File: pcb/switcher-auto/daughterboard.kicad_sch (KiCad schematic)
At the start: 6 parts, among them J0 MD-90SM, J1 MD-90SM, J2 MD-90SM, J3 MD-90SM, J4 MD-90SM, J5 Conn_02x22_Top_Bottom

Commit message: WIP routing as 4 layers with new connector organization
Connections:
- net 1_GND is gone; now on net 0_GND: J1.S1 (SHIELD), J1.S2 (SHIELD), J1.S3 (SHIELD), J5.16 (Pin_16)
- net 0_BVID: now also J5.6 (Pin_6); no longer J5.1 (Pin_1)
- net 0_CVID: now also J5.36 (Pin_36); no longer J5.4 (Pin_4)
- net 0_GND: now also J2.S1 (SHIELD), J2.S2 (SHIELD), J2.S3 (SHIELD), J3.S1 (SHIELD), J3.S2 (SHIELD), J3.S3 (SHIELD), J4.S1 (SHIELD), J4.S2 (SHIELD), J4.S3 (SHIELD), J5.17 (Pin_17), J5.18 (Pin_18), J5.19 (Pin_19), J5.20 (Pin_20); no longer J5.8 (Pin_8)
- net 0_GVID: now also J5.11 (Pin_11); no longer J5.2 (Pin_2)
- net 0_LAUD: now also J5.31 (Pin_31); no longer J5.5 (Pin_5)
- net 0_RAUD: now also J5.26 (Pin_26); no longer J5.6 (Pin_6)
- net 0_RVID: now also J5.1 (Pin_1); no longer J5.3 (Pin_3)
- net 1_BVID: now also J5.7 (Pin_7); no longer J5.9 (Pin_9)
- net 1_CVID: now also J5.37 (Pin_37); no longer J5.12 (Pin_12)
- net 1_GVID: now also J5.12 (Pin_12); no longer J5.10 (Pin_10)
- net 1_LAUD: now also J5.32 (Pin_32); no longer J5.13 (Pin_13)
- net 1_RAUD: now also J5.27 (Pin_27); no longer J5.14 (Pin_14)
- net 1_RVID: now also J5.2 (Pin_2); no longer J5.11 (Pin_11)
- net 2_BVID: now also J5.8 (Pin_8); no longer J5.33 (Pin_33)
- net 2_CVID: now also J5.38 (Pin_38); no longer J5.36 (Pin_36)
- net 2_GVID: now also J5.13 (Pin_13); no longer J5.34 (Pin_34)
- net 2_LAUD: now also J5.33 (Pin_33); no longer J5.37 (Pin_37)
- net 2_RAUD: now also J5.28 (Pin_28); no longer J5.38 (Pin_38)
- net 2_RVID: now also J5.3 (Pin_3); no longer J5.35 (Pin_35)
- net 3_BVID: now also J5.9 (Pin_9); no longer J5.25 (Pin_25)
- net 3_CVID: now also J5.39 (Pin_39); no longer J5.28 (Pin_28)
- net 3_GVID: now also J5.14 (Pin_14); no longer J5.26 (Pin_26)
- net 3_LAUD: now also J5.34 (Pin_34); no longer J5.29 (Pin_29)
- net 3_RAUD: now also J5.29 (Pin_29); no longer J5.30 (Pin_30)
- net 3_RVID: now also J5.4 (Pin_4); no longer J5.27 (Pin_27)
- net 4_BVID: now also J5.10 (Pin_10); no longer J5.17 (Pin_17)
- net 4_CVID: now also J5.40 (Pin_40); no longer J5.20 (Pin_20)
- net 4_GVID: now also J5.15 (Pin_15); no longer J5.18 (Pin_18)
- net 4_LAUD: now also J5.35 (Pin_35); no longer J5.21 (Pin_21)
- net 4_RAUD: now also J5.30 (Pin_30); no longer J5.22 (Pin_22)
- net 4_RVID: now also J5.5 (Pin_5); no longer J5.19 (Pin_19)
- net 0_5V renamed 0_VCC
- net 0_VCC: now also J5.21 (Pin_21); no longer J5.7 (Pin_7)
- net 1_5V renamed 1_VCC
- net 1_VCC: now also J5.22 (Pin_22); no longer J5.15 (Pin_15)
- net 2_5V renamed 2_VCC
- net 2_VCC: now also J5.23 (Pin_23); no longer J5.39 (Pin_39)
- removed net 2_GND: J2.S1 (SHIELD), J2.S2 (SHIELD), J2.S3 (SHIELD), J5.40 (Pin_40)
- net 3_5V renamed 3_VCC
- net 3_VCC: now also J5.24 (Pin_24); no longer J5.31 (Pin_31)
- removed net 3_GND: J3.S1 (SHIELD), J3.S2 (SHIELD), J3.S3 (SHIELD), J5.32 (Pin_32)
- net 4_5V renamed 4_VCC
- net 4_VCC: now also J5.25 (Pin_25); no longer J5.23 (Pin_23)
- removed net 4_GND: J4.S1 (SHIELD), J4.S2 (SHIELD), J4.S3 (SHIELD), J5.24 (Pin_24)

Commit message: Routing pt 2
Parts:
- added R1, R2, R3, R4, R5: R_Small, Resistor_SMD:R_0805_2012Metric_Pad1.20x1.40mm_HandSolder, symbol Device:R_Small
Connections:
- net 0_VCC: now also R5.1
- net 1_VCC: now also R4.1
- net 2_VCC: now also R3.1
- net 3_VCC: now also R2.1
- net 4_VCC: now also R1.1
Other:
- moved on the sheet: J4

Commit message: finish routing?
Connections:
- net 0_VCC: now also R5.2; no longer J5.21 (Pin_21), R5.1
- net 1_VCC: now also R4.2; no longer J5.22 (Pin_22), R4.1
- net 2_VCC: now also R3.2; no longer J5.23 (Pin_23), R3.1
- net 3_VCC: now also R2.2; no longer J5.24 (Pin_24), R2.1
- net 4_VCC: now also R1.2; no longer J5.25 (Pin_25), R1.1
- new net: J5.25 (Pin_25), R1.1
- new net: J5.23 (Pin_23), R3.1
- new net: J5.24 (Pin_24), R2.1
- new net: J5.22 (Pin_22), R4.1
- new net: J5.21 (Pin_21), R5.1
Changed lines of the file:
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@@
+    (effects (font (size 1.27 1.27)) (justify left bottom))
+  )
+  (label "3_VCC" (at 170.18 93.98 0) (fields_autoplaced)
     (effects (font (size 1.27 1.27)) (justify left bottom))
   )
@@
     (effects (font (size 1.27 1.27)) (justify right bottom))
   )
-  (label "3_VCC" (at 146.05 93.98 0) (fields_autoplaced)
-    (effects (font (size 1.27 1.27)) (justify left bottom))
-  )
   (label "0_LAUD" (at 104.14 66.04 0) (fields_autoplaced)
     (effects (font (size 1.27 1.27)) (justify left bottom))
@@
     (effects (font (size 1.27 1.27)) (justify left bottom))
   )
+  (label "2_VCC" (at 170.18 96.52 0) (fields_autoplaced)
+    (effects (font (size 1.27 1.27)) (justify left bottom))
+  )
   (label "1_GND" (at 133.35 93.98 180) (fields_autoplaced)
     (effects (font (size 1.27 1.27)) (justify right bottom))
@@
     (effects (font (size 1.27 1.27)) (justify left bottom))
   )
+  (label "4_VCC" (at 170.18 91.44 0) (fields_autoplaced)
+    (effects (font (size 1.27 1.27)) (justify left bottom))
+  )
   (label "0_RAUD" (at 146.05 88.9 0) (fields_autoplaced)
     (effects (font (size 1.27 1.27)) (justify left bottom))
@@
     (effects (font (size 1.27 1.27)) (justify left bottom))
   )
-  (label "2_VCC" (at 146.05 96.52 0) (fields_autoplaced)
-    (effects (font (size 1.27 1.27)) (justify left bottom))
-  )
   (label "1_GVID" (at 104.14 91.44 0) (fields_autoplaced)
     (effects (font (size 1.27 1.27)) (justify left bottom))
@@
     (effects (font (size 1.27 1.27)) (justify right bottom))
   )
+  (label "0_VCC" (at 170.18 101.6 0) (fields_autoplaced)
+    (effects (font (size 1.27 1.27)) (justify left bottom))
+  )
   (label "0_VCC" (at 104.14 50.8 0) (fields_autoplaced)
     (effects (font (size 1.27 1.27)) (justify left bottom))
@@
     (effects (font (size 1.27 1.27)) (justify right bottom))
   )
-  (label "4_VCC" (at 146.05 91.44 0) (fields_autoplaced)
-    (effects (font (size 1.27 1.27)) (justify left bottom))
-  )
-  (label "0_VCC" (at 146.05 101.6 0) (fields_autoplaced)
-    (effects (font (size 1.27 1.27)) (justify left bottom))
-  )
   (label "1_GVID" (at 133.35 81.28 180) (fields_autoplaced)
     (effects (font (size 1.27 1.27)) (justify right bottom))
@@
     (effects (font (size 1.27 1.27)) (justify right bottom))
   )
-  (label "1_VCC" (at 146.05 99.06 0) (fields_autoplaced)
-    (effects (font (size 1.27 1.27)) (justify left bottom))
-  )
+  (label "1_VCC" (at 170.18 99.06 0) (fields_autoplaced)
+    (effects (font (size 1.27 1.27)) (justify left bottom))
+  )

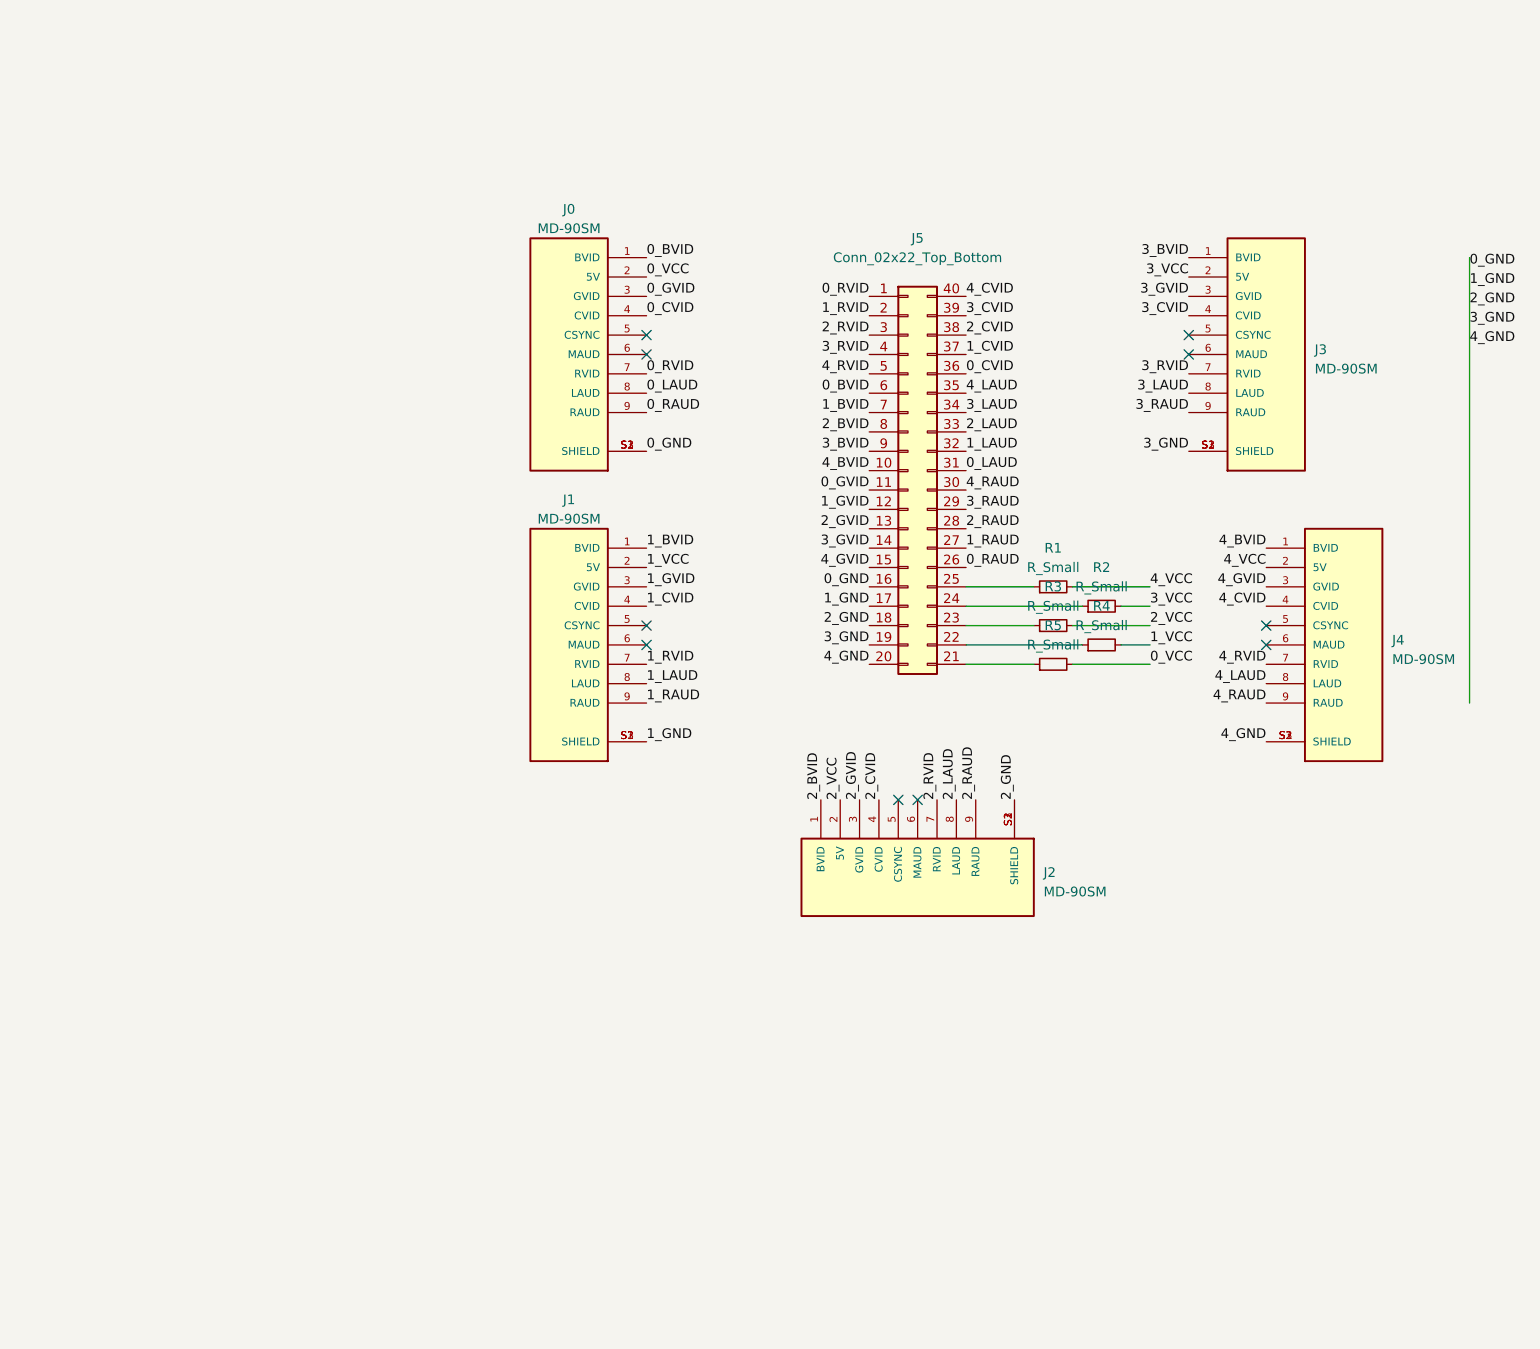
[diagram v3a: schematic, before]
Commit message: Adds daughterboard with adjustment options
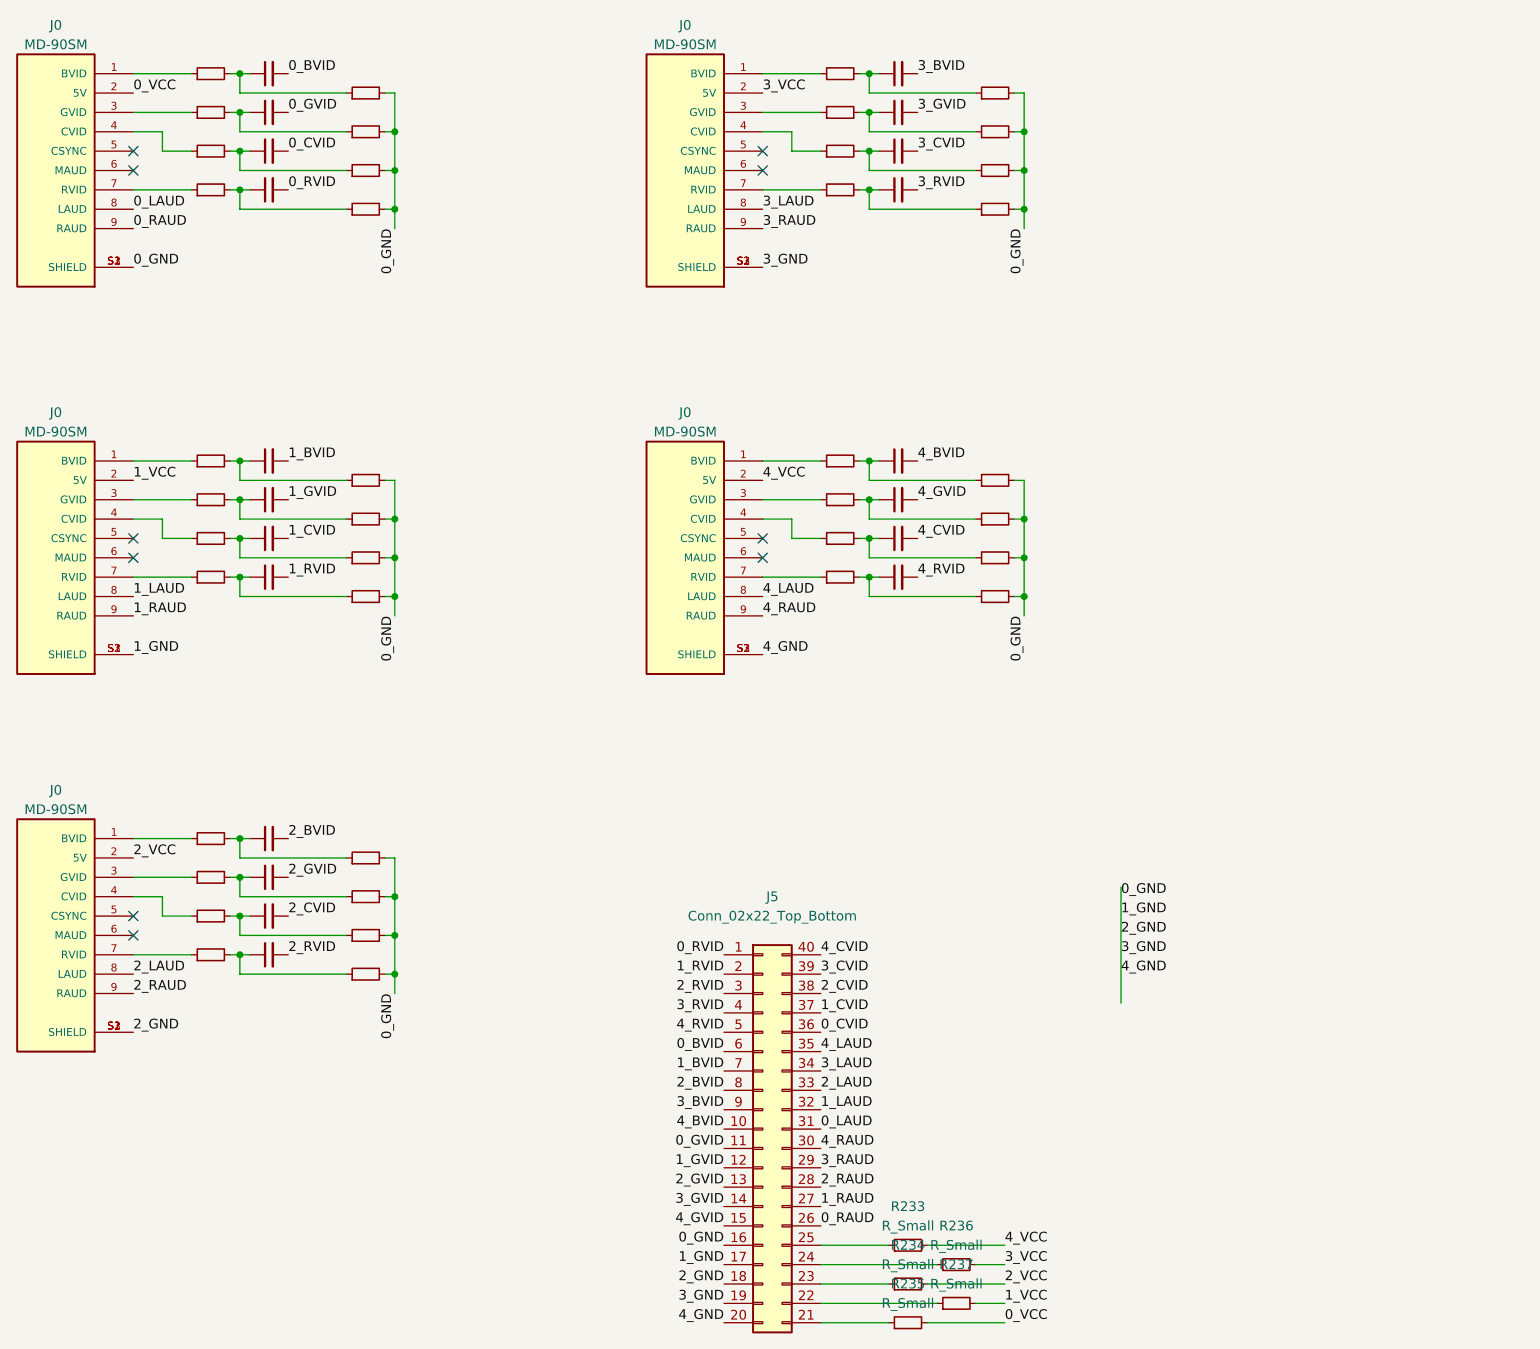
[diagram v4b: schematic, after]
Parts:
- removed J1, J2, J3, J4: MD-90SM, DIN9:CUI_MD-90SM, symbol DIN9:MD-90SM
- added C201, C202, C203, C204, C205, C206, C207, C208, C209, C210, C211, C212, C213, C214, C215, C216, C217, C218, C219, C220: C_Small, Capacitor_SMD:C_0805_2012Metric_Pad1.18x1.45mm_HandSolder, symbol Device:C_Small
- added J0 (x4): MD-90SM, DIN9:CUI_MD-90SM, symbol DIN9:MD-90SM
- added R201, R202, R203, R204, R205, R206, R207, R208, R209, R210, R211, R212, R213, R214, R215, R216, R217, R218, R219, R220, R221, R222, R223, R224, R225, R226, R227, R228, R229, R230, R231, R232, R238, R239, R240, R241, R242, R243, R244, R245: R_Small, Resistor_SMD:R_0805_2012Metric_Pad1.20x1.40mm_HandSolder, symbol Device:R_Small
- renumbered R1 to R233, R3 to R234, R5 to R235, R2 to R236, R4 to R237
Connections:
- net 0_BVID: now also C201.2; no longer J0.1 (BVID)
- net 0_CVID: now also C203.2; no longer J0.4 (CVID)
- net 0_GND: now also J0.S1 (SHIELD), J0.S1 (SHIELD), J0.S1 (SHIELD), J0.S1 (SHIELD), J0.S2 (SHIELD), J0.S2 (SHIELD), J0.S2 (SHIELD), J0.S2 (SHIELD), J0.S3 (SHIELD), J0.S3 (SHIELD), J0.S3 (SHIELD), J0.S3 (SHIELD), R213.2, R214.2, R215.2, R216.2, R217.2, R218.2, R219.2, R220.2, R221.2, R222.2, R223.2, R224.2, R238.2, R239.2, R240.2, R241.2, R242.2, R243.2, R244.2, R245.2
- net 0_GVID: now also C202.2; no longer J0.3 (GVID)
- net 0_RVID: now also C204.2; no longer J0.7 (RVID)
- net 1_BVID: now also C205.2
- net 1_CVID: now also C207.2
- net 1_GVID: now also C206.2
- net 1_LAUD: now also J0.8 (LAUD)
- net 1_RAUD: now also J0.9 (RAUD)
- net 1_RVID: now also C208.2
- net 1_VCC: now also J0.2 (5V)
- net 2_BVID: now also C209.2
- net 2_CVID: now also C211.2
- net 2_GVID: now also C210.2
- net 2_LAUD: now also J0.8 (LAUD)
- net 2_RAUD: now also J0.9 (RAUD)
- net 2_RVID: now also C212.2
- net 2_VCC: now also J0.2 (5V)
- net 3_BVID: now also C213.2
- net 3_CVID: now also C215.2
- net 3_GVID: now also C214.2
- net 3_LAUD: now also J0.8 (LAUD)
- net 3_RAUD: now also J0.9 (RAUD)
- net 3_RVID: now also C216.2
- net 3_VCC: now also J0.2 (5V)
- net 4_BVID: now also C217.2
- net 4_CVID: now also C219.2
- net 4_GVID: now also C218.2
- net 4_LAUD: now also J0.8 (LAUD)
- net 4_RAUD: now also J0.9 (RAUD)
- net 4_RVID: now also C220.2
- net 4_VCC: now also J0.2 (5V)
- new net: J0.3 (GVID), R202.1
- new net: C202.1, R202.2, R214.1
- new net: C219.1, R231.2, R244.1
- new net: J0.1 (BVID), R225.1
- new net: C213.1, R225.2, R238.1
- new net: C206.1, R206.2, R218.1
- new net: J0.1 (BVID), R229.1
- new net: C217.1, R229.2, R242.1
- new net: C215.1, R227.2, R240.1
- new net: J0.7 (RVID), R204.1
- new net: C204.1, R204.2, R216.1
- new net: J0.1 (BVID), R201.1
- new net: J0.4 (CVID), R203.1
- new net: J0.3 (GVID), R226.1
- new net: C214.1, R226.2, R239.1
- new net: J0.3 (GVID), R230.1
- new net: C218.1, R230.2, R243.1
- new net: C201.1, R201.2, R213.1
- new net: C203.1, R203.2, R215.1
- new net: J0.4 (CVID), R227.1
- new net: J0.7 (RVID), R228.1
- new net: C207.1, R207.2, R219.1
- new net: C211.1, R211.2, R223.1
- new net: J0.7 (RVID), R212.1
- new net: C212.1, R212.2, R224.1
- new net: C220.1, R232.2, R245.1
- new net: C210.1, R210.2, R222.1
- new net: J0.1 (BVID), R205.1
- new net: C205.1, R205.2, R217.1
- new net: J0.4 (CVID), R231.1
- new net: J0.3 (GVID), R206.1
- new net: J0.7 (RVID), R232.1
- new net: J0.4 (CVID), R207.1
- new net: C209.1, R209.2, R221.1
- new net: J0.1 (BVID), R209.1
- new net: J0.3 (GVID), R210.1
- new net: J0.4 (CVID), R211.1
- new net: C216.1, R228.2, R241.1
- new net: J0.7 (RVID), R208.1
- new net: C208.1, R208.2, R220.1
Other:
- moved on the sheet: J0, J5, R233, R234, R235, R236, R237

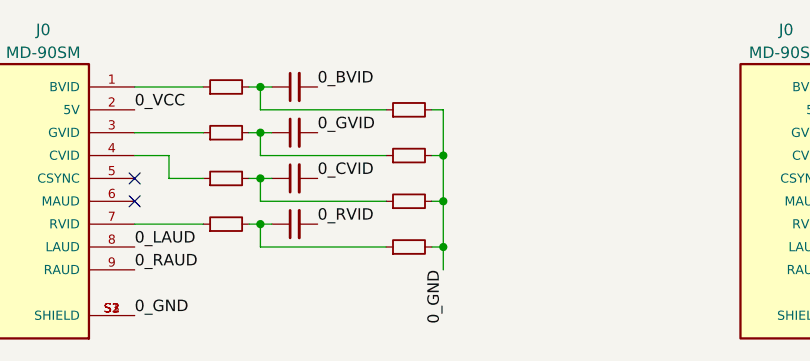
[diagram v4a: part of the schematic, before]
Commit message: Adds RGB breakout board standalone
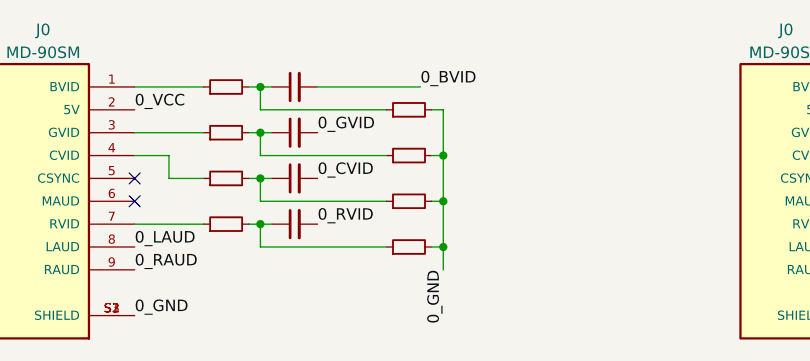
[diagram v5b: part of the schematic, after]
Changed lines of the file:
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@@
+    (stroke (width 0) (type default))
+  )
+  (wire (pts (xy 57.15 24.13) (xy 68.58 24.13))
     (stroke (width 0) (type default))
   )
@@
     (effects (font (size 1.27 1.27)) (justify left bottom))
   )
-  (label "0_BVID" (at 57.15 24.13 0) (fields_autoplaced)
-    (effects (font (size 1.27 1.27)) (justify left bottom))
-  )
+  (label "0_BVID" (at 68.58 24.13 0) (fields_autoplaced)
+    (effects (font (size 1.27 1.27)) (justify left bottom))
+  )
